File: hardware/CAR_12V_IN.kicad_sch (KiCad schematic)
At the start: 8 parts, among them J7 684M7W2103L461, Q26 AON7421, Q27 NMOS

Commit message: working on hardware
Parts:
- removed JP16, JP17: ~, symbol Jumper:SolderJumper_3_Open
- C112: renamed from C94; footprint (none) -> Capacitor_SMD:C_0603_1608Metric
- Q26: renamed from Q27; footprint (none) -> Package_TO_SOT_SMD:SOT-416
- Q27: renamed from Q26; footprint (none) -> Package_DFN_QFN:PQFN-8-EP_6x5mm_P1.27mm_Generic
- R104: renamed from R103; value 1M -> 330R
- renumbered J7 to J9, R100 to R105
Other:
- note added: "CAR CONNECTOR"
- note added: "SHELD LINK"
- moved on the sheet: C112, J9, Q26, Q27, R104, R105

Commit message: working assighning footprints still
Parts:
- R104, R105: footprint (none) -> Resistor_SMD:R_0603_1608Metric
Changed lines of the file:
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@@
       (effects (font (size 1.27 1.27)))
     )
-    (property "Footprint" "" (at 53.34 117.348 90)
+    (property "Footprint" "Resistor_SMD:R_0603_1608Metric" (at 53.34 117.348 90)
       (effects (font (size 1.27 1.27)) hide)
     )
@@
       (effects (font (size 1.27 1.27)) (justify left))
     )
-    (property "Footprint" "" (at 73.152 45.72 90)
+    (property "Footprint" "Resistor_SMD:R_0603_1608Metric" (at 73.152 45.72 90)
       (effects (font (size 1.27 1.27)) hide)
     )

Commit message: FINALY starting the pcb
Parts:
- J9: footprint (none) -> CARTHING:684M7W2103L461
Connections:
- net CAR_12V_IN: now also Q27.5 (D); no longer Q27.1 (D)
- net GND: now also Q26.2 (S); no longer Q26.3 (S)
- net at J9.1, Q27.3 (S), R105.1: now also Q27.1 (S), Q27.2 (S)
- net at J9.5: now also Q26.1 (G); no longer Q26.2 (G)
- new net: Q26.3 (D), Q27.4 (G), R105.2
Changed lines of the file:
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@@
       (effects (font (size 1.27 1.27)))
     )
-    (property "Footprint" "" (at 44.45 55.88 0)
+    (property "Footprint" "CARTHING:684M7W2103L461" (at 44.45 55.88 0)
       (effects (font (size 1.27 1.27)) hide)
     )
@@
       (effects (font (size 1.27 1.27)) hide)
     )
+    (pin "5")
     (pin "1")
+    (pin "3")
     (pin "2")
-    (pin "3")
+    (pin "4")
     (instances
       (project "usbc-car-module"
@@
       (effects (font (size 1.27 1.27)) hide)
     )
+    (pin "3")
     (pin "1")
     (pin "2")
-    (pin "3")
     (instances
       (project "usbc-car-module"

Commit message: finaliseing pcb layout will come back later for a fresh look
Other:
- company: (none) -> MICK MAKE
- title: (none) -> 200W USB PD 3.1 HUB
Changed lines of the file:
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@@
 (kicad_sch (version 20230121) (generator eeschema)
   (paper "A4")
+  (title_block
+    (title "200W USB PD 3.1 HUB")
+    (date "2023-10-03")
+    (rev "A")
+    (company "MICK MAKE")
+    (comment 1 "THIS IS A 2X 100W USB PD SOURCE ")
+    (comment 2 "HUB USB SPEC 3.1")
+    (comment 3 "TOTAL SYSTEM POWER IS ~275w")
+  )
   (junction (at 62.23 115.57) (diameter 0) (color 0 0 0 0)
   )

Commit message: fialiseing pcb for production
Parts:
- added H1 (x9): MountingHole, MountingHole:MountingHole_3.2mm_M3, symbol Mechanical:MountingHole
- added R107: 100K, Resistor_SMD:R_0603_1608Metric, symbol Device:R
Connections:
- net GND: now also R107.2
- net at J9.5, Q26.1 (G): now also R107.1
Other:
- note added: "MOUNTING HOLES"

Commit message: minor revisions
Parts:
- Q26: value NMOS -> NTA7002NT1G
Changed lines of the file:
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@@
       (effects (font (size 1.27 1.27)) (justify left))
     )
-    (property "Value" "NMOS" (at 90.297 59.6973 0)
+    (property "Value" "NTA7002NT1G" (at 90.297 59.6973 0)
       (effects (font (size 1.27 1.27)) (justify left))
     )

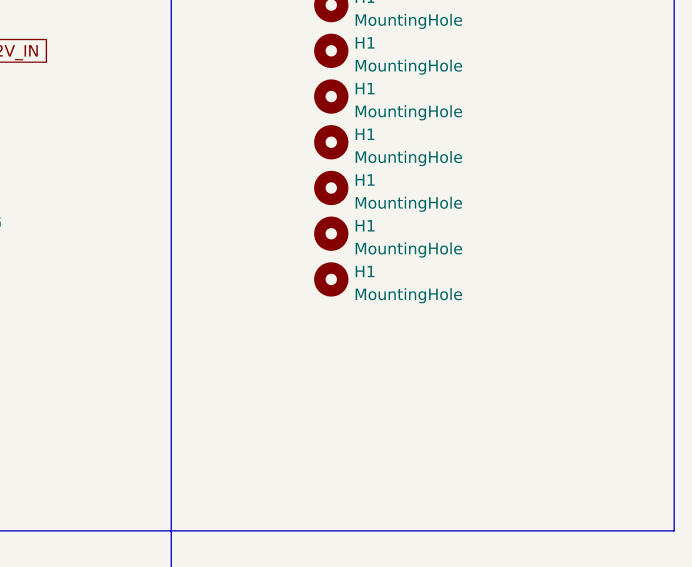
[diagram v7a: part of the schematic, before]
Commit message: updated block digram minor pcb changes
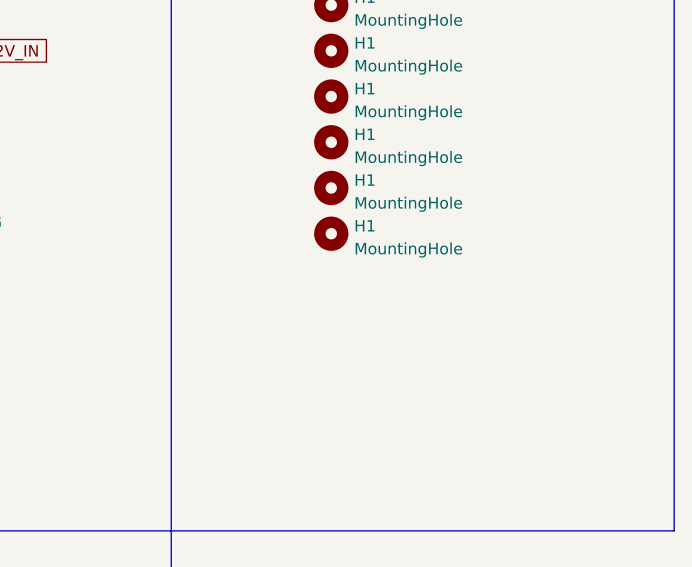
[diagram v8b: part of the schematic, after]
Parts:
- removed H1: MountingHole, MountingHole:MountingHole_3.2mm_M3, symbol Mechanical:MountingHole
